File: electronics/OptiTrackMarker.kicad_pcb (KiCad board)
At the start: 2 copper layers, 48.3 x 25.4 mm, 9 parts, among them J5 Conn_01x02_Socket, J6 Conn_01x02_Socket, J7 Conn_01x02_Socket, J8 Conn_01x02_Socket, SW1 SW_SPDT, U1 XIAO-ESP32-C6-SMD, U2 TLC5917QDRQ1

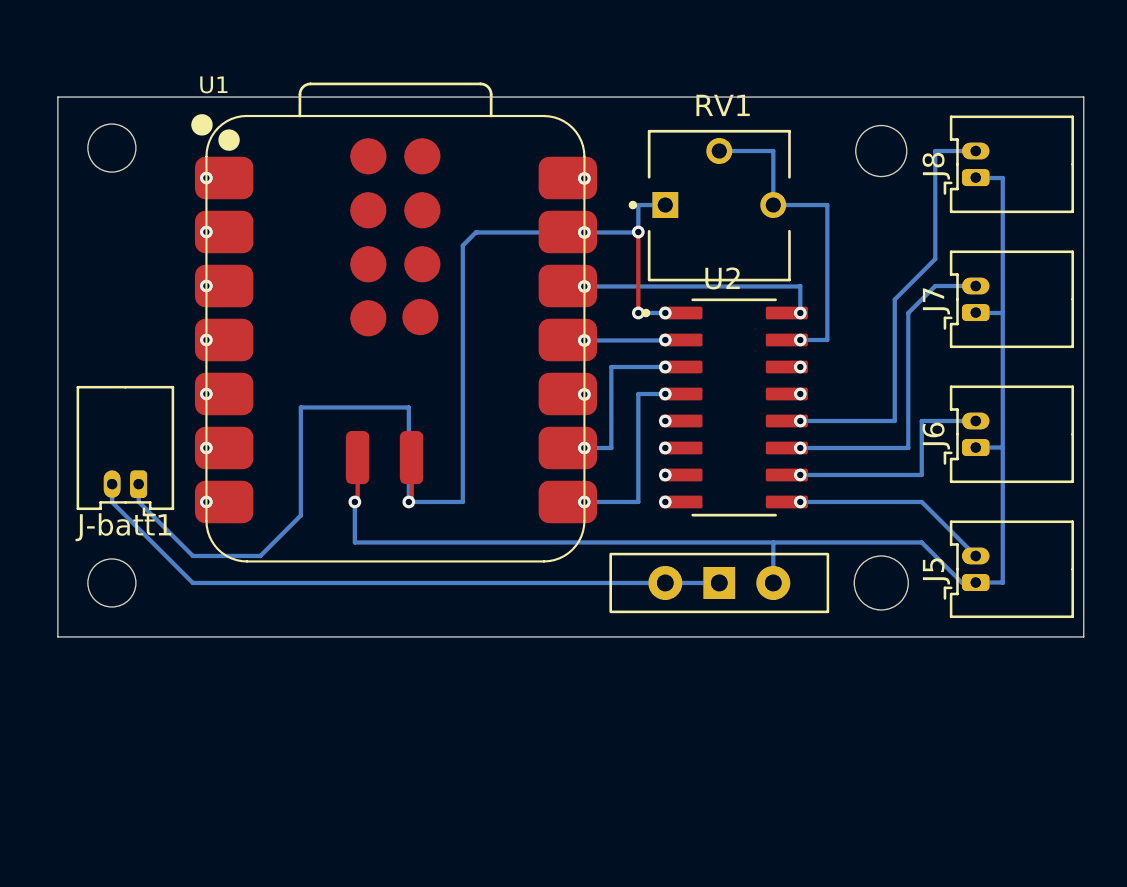
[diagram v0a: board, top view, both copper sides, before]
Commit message: [WIP@ele] connector layout change
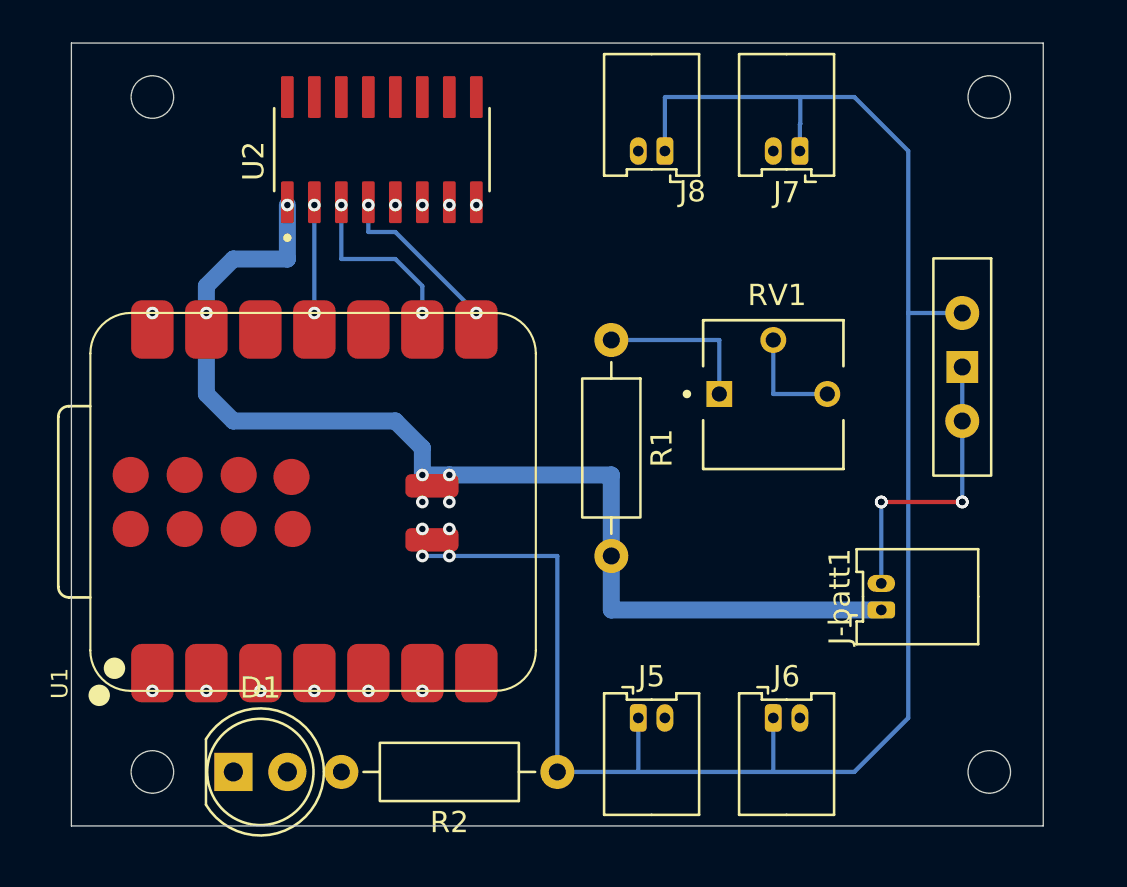
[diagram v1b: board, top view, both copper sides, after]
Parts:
- added D1: LED, LED_THT:LED_D5.0mm, F.Cu at (40.6, 66.0)
- added R1: R, Resistor_THT:R_Axial_DIN0207_L6.3mm_D2.5mm_P10.16mm_Horizontal, F.Cu at (58.4, 45.7)
- added R2: 470, Resistor_THT:R_Axial_DIN0207_L6.3mm_D2.5mm_P10.16mm_Horizontal, F.Cu at (55.9, 66.0)
- moved J-batt1 35.4 mm to (71.1, 58.4), turned to 90 degrees
- moved U2 20.5 mm to (47.6, 36.8), turned to 90 degrees
- moved J5 17.1 mm to (59.7, 63.5), turned to 0 degrees
- moved J6 15.9 mm to (66.0, 63.5), turned to 0 degrees
- moved SW1 15.3 mm to (74.9, 47.0), turned to -90 degrees
- moved J8 14.7 mm to (60.9, 36.8), turned to 180 degrees
- moved J7 11.2 mm to (67.3, 36.8), turned to 180 degrees
- moved RV1 9.25 mm to (66.0, 48.3)
- moved U1 8.45 mm to (44.4, 53.1), turned to 90 degrees
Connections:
- RV1 pad 1: GND -> Net-(R1-Pad1)
- U1 pad 1: unconnected-(U1-GPIO0_A0_D0-Pad1) -> Net-(D1-K)
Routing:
- net +BATT: track 60.1 -> 85.9 mm, vias 1 -> 4
- net Net-(J8-Pin_2): track 19.8 -> 0.00 mm, vias 1 -> 0
- net Net-(J-batt1-Pin_2): track 31.0 -> 14.0 mm, vias 0 -> 4
- net Net-(J7-Pin_2): track 15.1 -> 0.00 mm, vias 1 -> 0
- net Net-(U1-3V3): track 11.4 -> 0.00 mm, vias 2 -> 0
- net Net-(J6-Pin_2): track 10.8 -> 0.00 mm, vias 1 -> 0
- net Net-(U2-R-EXT): track 15.2 -> 5.08 mm, vias 1 -> 0
- net Net-(J5-Pin_2): track 9.31 -> 0.00 mm, vias 1 -> 0
- net Net-(R1-Pad1): track 0.00 -> 7.62 mm
- net GND: track 57.8 -> 52.4 mm, vias 5 -> 6
- net Net-(U1-GPIO18_D10_MOSI): track 3.85 -> 5.08 mm
- net Net-(U1-GPIO17_D7_RX): track 8.89 -> 7.93 mm
- net Net-(U1-GPIO19_D8_SCK): track 7.62 -> 8.15 mm
- net unconnected-(U1-GPIO0_A0_D0-Pad1): vias 1 -> 0
- net Net-(U1-GPIO20_D9_MISO): vias 2 -> 0
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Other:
- board size 48.3 x 25.4 mm -> 45.7 x 36.8 mm
- copper layers 2 -> 4

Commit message: [WIP] in prgress, copy real circuit..
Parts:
- removed D1: LED, LED_THT:LED_D5.0mm
- removed J-batt1, J5, J6, J7, J8: Conn_01x02_Socket, Library:Molex_PicoBlade_53048-0210_1x02_P1.25mm_Horizontal_2
- added D2: LED_RKBG, LED_THT:LED_D5.0mm-4_RGB, F.Cu at (39.4, 66.0)
- added J1: Conn_01x03_Socket, Connector_Molex:Molex_PicoBlade_53048-0310_1x03_P1.25mm_Horizontal, F.Cu at (68.6, 63.5)
- added J2: Conn_01x03_Socket, Connector_Molex:Molex_PicoBlade_53048-0310_1x03_P1.25mm_Horizontal, F.Cu at (59.7, 63.5)
- added J3: Conn_01x03_Socket, Connector_Molex:Molex_PicoBlade_53048-0310_1x03_P1.25mm_Horizontal, F.Cu at (71.1, 36.8)
- added J4: Conn_01x03_Socket, Connector_Molex:Molex_PicoBlade_53048-0310_1x03_P1.25mm_Horizontal, F.Cu at (62.2, 36.8)
- added J9: Conn_01x03_Socket, Connector_Molex:Molex_PicoBlade_53048-0310_1x03_P1.25mm_Horizontal, F.Cu at (69.8, 57.1)
- added R3: 150, Resistor_THT:R_Axial_DIN0207_L6.3mm_D2.5mm_P10.16mm_Horizontal, F.Cu at (45.7, 67.3)
- R2: value 470 -> 22
- moved RV1 4.02 mm to (62.2, 49.5)
- moved R2 1.27 mm to (55.9, 64.8)
- moved SW1 1.27 mm to (73.7, 47.0)
- moved R1 1.27 mm to (57.1, 45.7)
- moved U2 0.63 mm to (48.3, 36.8)
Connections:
- R2 pad 1: +BATT -> Net-(U1-GPIO1_A1_D1)
- U1 pad 2: unconnected-(U1-GPIO1_A1_D1-Pad2) -> Net-(U1-GPIO1_A1_D1)
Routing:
- net Net-(U1-GPIO17_D7_RX): track 7.93 -> 11.1 mm, vias 2 -> 0
- net Net-(R1-Pad1): track 7.62 -> 4.86 mm
- net Net-(J9-Pin_3): track 14.0 -> 11.5 mm, vias 4 -> 0
- net +BATT: track 85.9 -> 83.6 mm, vias 4 -> 0
- net GND: track 52.4 -> 50.4 mm, vias 6 -> 0
- net Net-(U1-GPIO19_D8_SCK): track 8.15 -> 9.80 mm, vias 2 -> 0
- net Net-(U2-R-EXT): track 5.08 -> 3.59 mm
- net Net-(U1-GPIO18_D10_MOSI): track 5.08 -> 5.99 mm, vias 2 -> 0
- net unconnected-(U2-OUT3-Pad8): vias 1 -> 0
- net unconnected-(U2-OUT2-Pad7): vias 1 -> 0
- net unconnected-(U2-OUT1-Pad6): vias 1 -> 0
- net unconnected-(U2-OUT0-Pad5): vias 1 -> 0
- net unconnected-(U1-GPIO2_A2_D2-Pad3): vias 1 -> 0
- net unconnected-(U1-GPIO23_D5_SCL-Pad6): vias 1 -> 0
- net unconnected-(U1-GPIO22_D4_SDA-Pad5): vias 1 -> 0
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
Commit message: [WIP] 青色LEDで動作確認まで完了
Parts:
- added R4: 22, Resistor_THT:R_Axial_DIN0207_L6.3mm_D2.5mm_P10.16mm_Horizontal, F.Cu at (41.9, 58.4)
- added R5: 22, Resistor_THT:R_Axial_DIN0207_L6.3mm_D2.5mm_P10.16mm_Horizontal, F.Cu at (52.1, 61.0)
- moved D2 44.9 mm to (72.4, 35.6), turned to 180 degrees
- moved J3 41.3 mm to (40.7, 64.8), turned to 0 degrees
- moved SW1 36.4 mm to (38.1, 54.6), turned to 90 degrees
- moved J1 35.9 mm to (43.2, 38.1), turned to 180 degrees
- moved R3 34.5 mm to (55.9, 34.3)
- moved U2 31.9 mm to (63.5, 64.8), turned to -90 degrees
- moved J4 30.7 mm to (49.5, 64.8), turned to 0 degrees
- moved J9 30.7 mm to (41.9, 44.5), turned to -90 degrees
- moved R2 27.9 mm to (55.9, 36.8), turned to 0 degrees
- moved J2 26.5 mm to (52.0, 38.1), turned to 180 degrees
- moved U1 23.4 mm to (67.3, 48.3), turned to -90 degrees
- moved RV1 13.0 mm to (49.5, 52.1), turned to 180 degrees
- moved R1 10.5 mm to (54.6, 55.9), turned to 90 degrees
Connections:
- R2 pad 1: Net-(U1-GPIO1_A1_D1) -> Net-(U1-GPIO23_D5_SCL)
- R3 pad 1: Net-(U1-GPIO0_A0_D0) -> Net-(U1-GPIO22_D4_SDA)
- U1 pad 2: Net-(U1-GPIO1_A1_D1) -> unconnected-(U1-GPIO1_A1_D1-Pad2)
- U1 pad 5: unconnected-(U1-GPIO22_D4_SDA-Pad5) -> Net-(U1-GPIO22_D4_SDA)
- U1 pad 6: unconnected-(U1-GPIO23_D5_SCL-Pad6) -> Net-(U1-GPIO23_D5_SCL)
- U2 pad 10: Net-(J2-Pin_3) -> Net-(J3-Pin_3)
- U2 pad 11: Net-(J3-Pin_3) -> Net-(J1-Pin_3)
- U2 pad 12: Net-(J4-Pin_3) -> Net-(J2-Pin_3)
- U2 pad 9: Net-(J1-Pin_3) -> Net-(J4-Pin_3)
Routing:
- net GND: track 50.4 -> 92.9 mm
- net Net-(U2-R-EXT): track 3.59 -> 28.1 mm
- net Net-(J3-Pin_3): track 0.00 -> 23.2 mm
- net Net-(U1-GPIO22_D4_SDA): track 0.00 -> 12.5 mm
- net Net-(J4-Pin_3): track 0.00 -> 10.2 mm
- net Net-(D2-RA): track 0.00 -> 7.62 mm
- net Net-(D2-GA): track 0.00 -> 3.81 mm
- net Net-(U1-GPIO0_A0_D0): track 0.00 -> 2.54 mm
- net +BATT: track 83.6 -> 86.2 mm
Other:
- outline, holes or cut-outs redrawn

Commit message: [ele] v2 layout draft
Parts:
- added J5: Conn_01x02_Socket, Connector_Molex:Molex_PicoBlade_53048-0210_1x02_P1.25mm_Horizontal, F.Cu at (92.7, 49.3)
- added J6: Conn_01x02_Socket, Connector_Molex:Molex_PicoBlade_53048-0210_1x02_P1.25mm_Horizontal, F.Cu at (98.3, 49.3)
- added J7: Conn_01x02_Socket, Connector_Molex:Molex_PicoBlade_53048-0210_1x02_P1.25mm_Horizontal, F.Cu at (103.9, 49.3)
- added J8: Conn_01x02_Socket, Connector_Molex:Molex_PicoBlade_53048-0210_1x02_P1.25mm_Horizontal, F.Cu at (109.5, 49.3)
- J1, J2, J3, J4: value Conn_01x03_Socket -> Conn_01x02_Socket; footprint Connector_Molex:Molex_PicoBlade_53048-0310_1x03_P1.25mm_Horizontal -> Connector_Molex:Molex_PicoBlade_53048-0210_1x02_P1.25mm_Horizontal
- R1, R4, R5: footprint Resistor_THT:R_Axial_DIN0207_L6.3mm_D2.5mm_P10.16mm_Horizontal -> Resistor_SMD:R_0603_1608Metric_Pad0.98x0.95mm_HandSolder; moved to B.Cu
- RV1: footprint Snapeda:TRIM_3362P-1-103 -> Potentiometer_SMD:Potentiometer_Bourns_TC33X_Vertical
- moved R3 78.4 mm to (134.1, 28.6)
- moved R4 73.3 mm to (111.8, 36.1)
- moved R5 72.1 mm to (118.1, 32.1), turned to 90 degrees
- moved J1 67.8 mm to (111.0, 38.1)
- moved J3 64.6 mm to (99.6, 38.1), turned to 180 degrees
- moved D2 59.2 mm to (130.4, 24.0)
- moved U1 57.9 mm to (125.1, 44.3)
- moved R2 56.4 mm to (111.4, 27.1)
- moved J2 53.1 mm to (105.2, 38.1)
- moved J4 51.8 mm to (94.0, 38.1), turned to 180 degrees
- moved RV1 51.5 mm to (100.3, 43.7), turned to 90 degrees
- moved U2 48.9 mm to (107.6, 43.6)
- moved R1 48.8 mm to (101.6, 42.7), turned to -90 degrees
- moved SW1 5.09 mm to (33.7, 52.1)
- moved J9 5.09 mm to (37.5, 42.0)
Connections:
- J1 pad 2: unconnected-(J1-Pin_2-Pad2) -> Net-(J1-Pin_2)
- J2 pad 2: unconnected-(J2-Pin_2-Pad2) -> Net-(J2-Pin_2)
- J3 pad 2: unconnected-(J3-Pin_2-Pad2) -> Net-(J3-Pin_2)
- J4 pad 2: unconnected-(J4-Pin_2-Pad2) -> Net-(J4-Pin_2)
- RV1 pad 2: Net-(U2-R-EXT) -> Net-(R1-Pad1)
- U2 pad 10: Net-(J3-Pin_3) -> Net-(J6-Pin_2)
- U2 pad 11: Net-(J1-Pin_3) -> Net-(J7-Pin_2)
- U2 pad 12: Net-(J2-Pin_3) -> Net-(J8-Pin_2)
- U2 pad 5: unconnected-(U2-OUT0-Pad5) -> Net-(J1-Pin_2)
- U2 pad 6: unconnected-(U2-OUT1-Pad6) -> Net-(J2-Pin_2)
- U2 pad 7: unconnected-(U2-OUT2-Pad7) -> Net-(J3-Pin_2)
- U2 pad 8: unconnected-(U2-OUT3-Pad8) -> Net-(J4-Pin_2)
- U2 pad 9: Net-(J4-Pin_3) -> Net-(J5-Pin_2)
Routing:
- net GND: track 92.9 -> 9.08 mm, vias 0 -> 1
- net Net-(U1-3V3): track 0.00 -> 26.9 mm, vias 0 -> 1
- net Net-(U1-GPIO20_D9_MISO): track 0.00 -> 24.0 mm
- net Net-(J3-Pin_3): track 23.2 -> 0.00 mm
- net Net-(U2-R-EXT): track 28.1 -> 10.6 mm
- net +BATT: track 86.2 -> 69.1 mm, vias 0 -> 1
- net Net-(U1-GPIO18_D10_MOSI): track 5.99 -> 20.6 mm
- net Net-(U1-GPIO22_D4_SDA): track 12.5 -> 0.00 mm
- net Net-(J4-Pin_2): track 0.00 -> 11.7 mm
- net Net-(J9-Pin_3): track 11.4 -> 0.00 mm
- net Net-(J5-Pin_2): track 0.00 -> 10.5 mm
- net Net-(J4-Pin_3): track 10.2 -> 0.00 mm
- net Net-(J3-Pin_2): track 0.00 -> 7.79 mm
- net Net-(D2-RA): track 7.62 -> 0.00 mm
- net Net-(U1-GPIO19_D8_SCK): track 9.80 -> 16.6 mm
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
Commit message: [WIP]
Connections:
- U1 pad 10: Net-(U1-GPIO20_D9_MISO) -> unconnected-(U1-GPIO20_D9_MISO-Pad10)
- U2 pad 14: Net-(U1-GPIO20_D9_MISO) -> GND
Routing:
- net Net-(U1-GPIO20_D9_MISO): track 24.0 -> 0.00 mm
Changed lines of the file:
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@@
 	(net 6 "unconnected-(U1-MTMS-Pad21)")
 	(net 7 "Net-(U1-GPIO17_D7_RX)")
-	(net 8 "Net-(U1-GPIO20_D9_MISO)")
+	(net 8 "unconnected-(U1-GPIO20_D9_MISO-Pad10)")
 	(net 9 "Net-(U1-GPIO19_D8_SCK)")
 	(net 10 "unconnected-(U1-5V-Pad14)")
@@
 			(layers "F.Cu" "F.Mask" "F.Paste")
 			(roundrect_rratio 0.125)
-			(net 8 "Net-(U1-GPIO20_D9_MISO)")
+			(net 1 "GND")
 			(pinfunction "SDO")
 			(pintype "output")
@@
 			(layers "F.Cu" "F.Mask" "F.Paste")
 			(roundrect_rratio 0.25)
-			(net 8 "Net-(U1-GPIO20_D9_MISO)")
+			(net 8 "unconnected-(U1-GPIO20_D9_MISO-Pad10)")
 			(pinfunction "GPIO20_D9_MISO")
 			(pintype "passive")
@@
 	)
 	(segment
-		(start 120.879 53.909)
-		(end 116.393 53.909)
-		(width 0.2)
-		(layer "F.Cu")
-		(net 8)
-	)
-	(segment
-		(start 111.361 45.030176)
-		(end 111.361 47.165824)
-		(width 0.2)
-		(layer "F.Cu")
-		(net 8)
-	)
-	(segment
-		(start 122.555 52.233)
-		(end 122.555 52.197)
-		(width 0.2)
-		(layer "F.Cu")
-		(net 8)
-	)
-	(segment
-		(start 111.579176 44.812)
-		(end 111.361 45.030176)
-		(width 0.2)
-		(layer "F.Cu")
-		(net 8)
-	)
-	(segment
-		(start 116.393 53.909)
-		(end 112.631 50.147)
-		(width 0.2)
-		(layer "F.Cu")
-		(net 8)
-	)
-	(segment
-		(start 111.361 47.165824)
-		(end 111.142824 47.384)
-		(width 0.2)
-		(layer "F.Cu")
-		(net 8)
-	)
-	(segment
-		(start 111.142824 47.384)
-		(end 109.791001 47.384)
-		(width 0.2)
-		(layer "F.Cu")
-		(net 8)
-	)
-	(segment
-		(start 122.555 52.233)
-		(end 120.879 53.909)
-		(width 0.2)
-		(layer "F.Cu")
-		(net 8)
-	)
-	(segment
-		(start 109.49 47.082999)
-		(end 109.49 46.098)
-		(width 0.2)
-		(layer "F.Cu")
-		(net 8)
-	)
-	(segment
-		(start 112.631 45.030176)
-		(end 112.412824 44.812)
-		(width 0.2)
-		(layer "F.Cu")
-		(net 8)
-	)
-	(segment
-		(start 112.412824 44.812)
-		(end 111.579176 44.812)
-		(width 0.2)
-		(layer "F.Cu")
-		(net 8)
-	)
-	(segment
-		(start 112.631 50.147)
-		(end 112.631 45.030176)
-		(width 0.2)
-		(layer "F.Cu")
-		(net 8)
-	)
-	(segment
-		(start 109.791001 47.384)
-		(end 109.49 47.082999)
-		(width 0.2)
-		(layer "F.Cu")
-		(net 8)
-	)
-	(segment
